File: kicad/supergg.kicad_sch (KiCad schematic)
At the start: 13 parts, among them J1 Conn_01x04_Pin, U1 Pin_Connector, U2 Edge_Connector, U3 STM32F103C8Tx, U4 XC6206P332MR

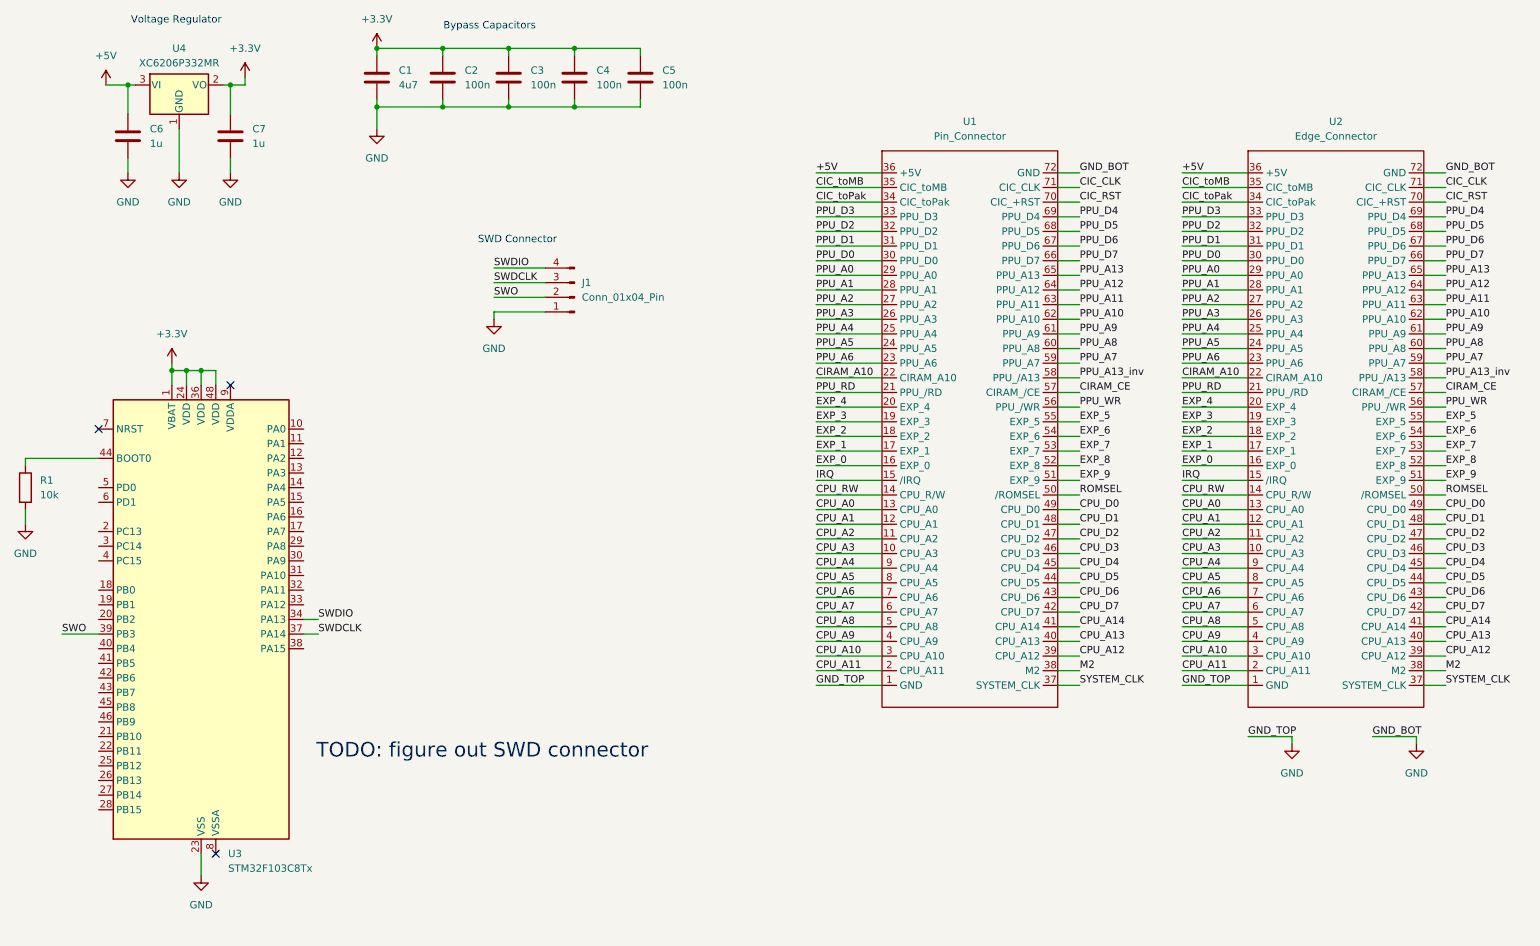
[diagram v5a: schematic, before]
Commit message: finish first draft of wiring
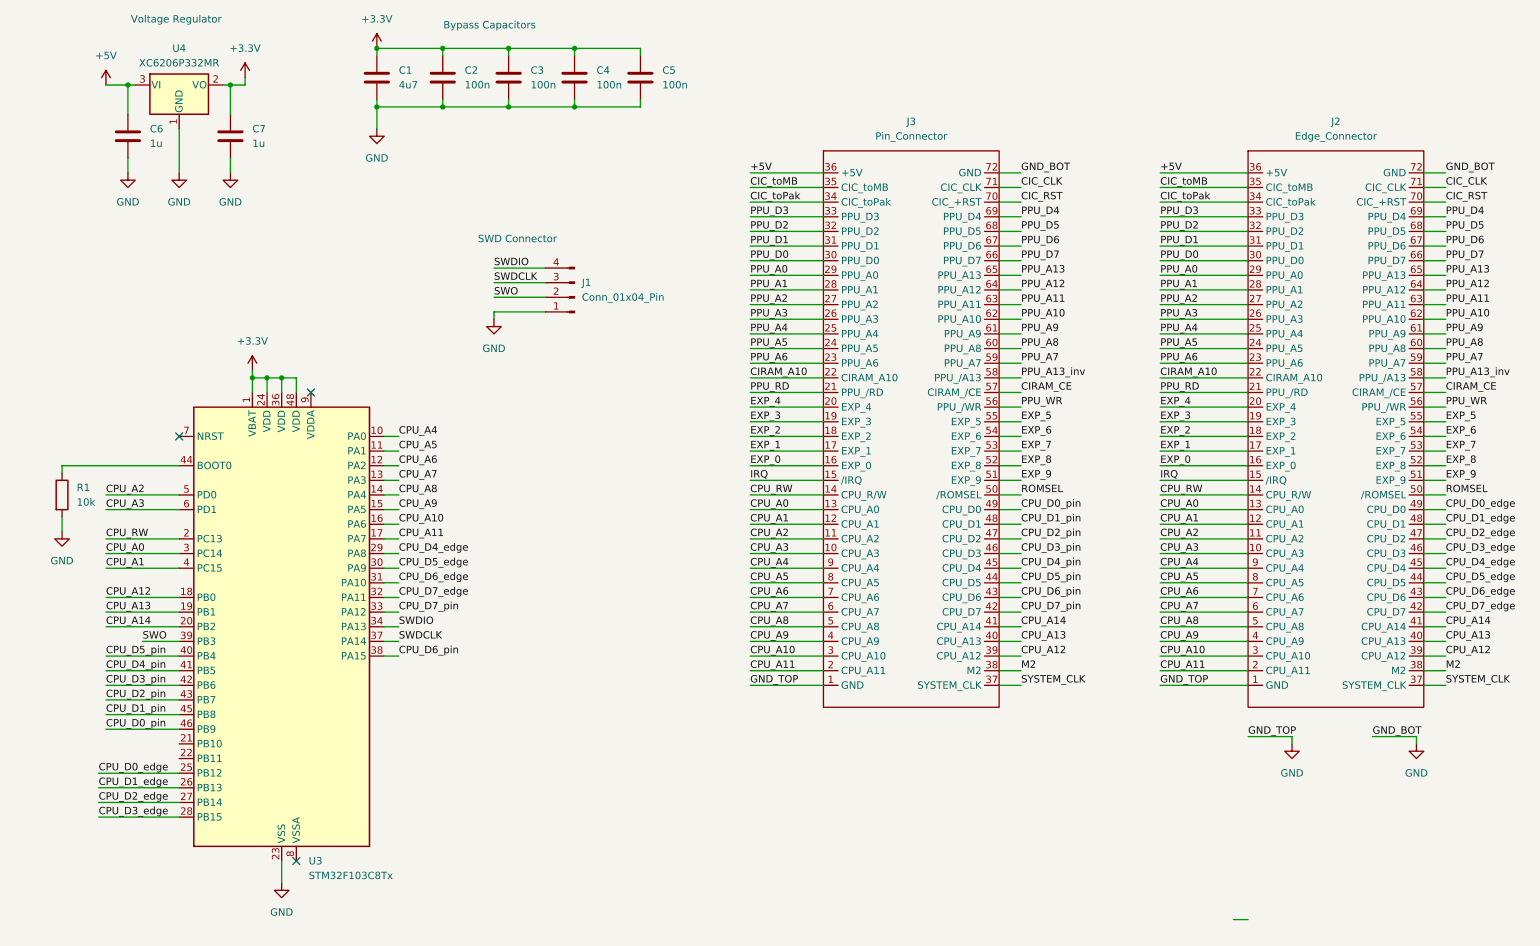
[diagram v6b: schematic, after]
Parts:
- C1: LCSC (none) -> C1705
- C2, C3, C4, C5: LCSC (none) -> C1525
- C6, C7: LCSC (none) -> C1592
- J1: LCSC (none) -> C492412
- R1: LCSC (none) -> C25804
- U3: LCSC (none) -> C8734
- U4: LCSC (none) -> C347376
- renumbered U2 to J2, U1 to J3
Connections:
- net CPU_A0: now also U3.3 (PC14)
- net CPU_A1: now also U3.4 (PC15)
- net CPU_A10: now also U3.16 (PA6)
- net CPU_A11: now also U3.17 (PA7)
- net CPU_A12: now also U3.18 (PB0)
- net CPU_A13: now also U3.19 (PB1)
- net CPU_A14: now also U3.20 (PB2)
- net CPU_A2: now also U3.5 (PD0)
- net CPU_A3: now also U3.6 (PD1)
- net CPU_A4: now also U3.10 (PA0)
- net CPU_A5: now also U3.11 (PA1)
- net CPU_A6: now also U3.12 (PA2)
- net CPU_A7: now also U3.13 (PA3)
- net CPU_A8: now also U3.14 (PA4)
- net CPU_A9: now also U3.15 (PA5)
- net CPU_RW: now also U3.2 (PC13)
- net CPU_D0_edge: now reaches U3.25 (PB12)
- net CPU_D0_edge: now also J2.49 (CPU_D0)
- net CPU_D1_edge: now reaches U3.26 (PB13)
- net CPU_D1_edge: now also J2.48 (CPU_D1)
- net CPU_D2_edge: now reaches U3.27 (PB14)
- net CPU_D2_edge: now also J2.47 (CPU_D2)
- net CPU_D3_edge: now reaches U3.28 (PB15)
- net CPU_D3_edge: now also J2.46 (CPU_D3)
- net CPU_D4_edge: now reaches U3.29 (PA8)
- net CPU_D4_edge: now also J2.45 (CPU_D4)
- net CPU_D5_edge: now reaches U3.30 (PA9)
- net CPU_D5_edge: now also J2.44 (CPU_D5)
- net CPU_D6_edge: now reaches U3.31 (PA10)
- net CPU_D6_edge: now also J2.43 (CPU_D6)
- net CPU_D7_edge: now reaches U3.32 (PA11)
- net CPU_D7_edge: now also J2.42 (CPU_D7)
- net CPU_D7_pin: now reaches U3.33 (PA12)
- net CPU_D7_pin: now also J3.42 (CPU_D7)
- net CPU_D6_pin: now reaches U3.38 (PA15)
- net CPU_D6_pin: now also J3.43 (CPU_D6)
- net CPU_D5_pin: now reaches U3.40 (PB4)
- net CPU_D5_pin: now also J3.44 (CPU_D5)
- net CPU_D4_pin: now reaches U3.41 (PB5)
- net CPU_D4_pin: now also J3.45 (CPU_D4)
- net CPU_D3_pin: now reaches U3.42 (PB6)
- net CPU_D3_pin: now also J3.46 (CPU_D3)
- net CPU_D2_pin: now reaches U3.43 (PB7)
- net CPU_D2_pin: now also J3.47 (CPU_D2)
- net CPU_D1_pin: now reaches U3.45 (PB8)
- net CPU_D1_pin: now also J3.48 (CPU_D1)
- net CPU_D0_pin: now reaches U3.46 (PB9)
- net CPU_D0_pin: now also J3.49 (CPU_D0)
- removed net CPU_D0: J2.49 (CPU_D0), J3.49 (CPU_D0)
- removed net CPU_D1: J2.48 (CPU_D1), J3.48 (CPU_D1)
- removed net CPU_D2: J2.47 (CPU_D2), J3.47 (CPU_D2)
- removed net CPU_D3: J2.46 (CPU_D3), J3.46 (CPU_D3)
- removed net CPU_D4: J2.45 (CPU_D4), J3.45 (CPU_D4)
- removed net CPU_D5: J2.44 (CPU_D5), J3.44 (CPU_D5)
- removed net CPU_D6: J2.43 (CPU_D6), J3.43 (CPU_D6)
- removed net CPU_D7: J2.42 (CPU_D7), J3.42 (CPU_D7)
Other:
- note removed: "TODO: figure out SWD connector"
- moved on the sheet: J3, R1, U3
